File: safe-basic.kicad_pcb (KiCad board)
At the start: 10 x 10 mm, 1 part

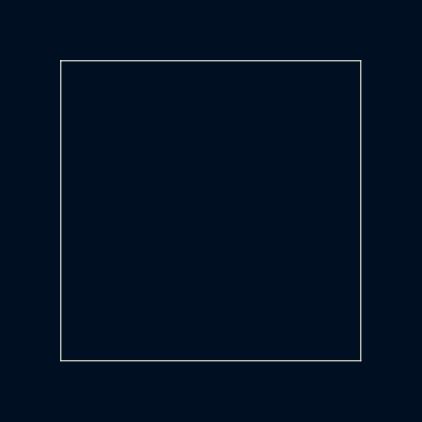
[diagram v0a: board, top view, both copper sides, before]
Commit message: test: source-authentic KiCad DRC track markers for #1161
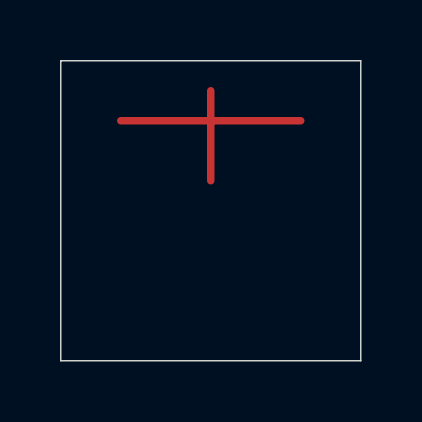
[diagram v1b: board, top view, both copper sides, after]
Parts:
- removed R1: , Resistor_SMD:R_0603
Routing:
- net NET_A: track 0.00 -> 6.00 mm
- net NET_B: track 0.00 -> 3.00 mm
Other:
- copper layers 0 -> 2
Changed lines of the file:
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@@
 (kicad_pcb
   (version 20250114)
-  (title_block (title "safe-basic") (rev "v1.0"))
-  (gr_rect (start 0 0) (end 10 10) (layer "Edge.Cuts"))
-  (footprint "Resistor_SMD:R_0603"
-    (property "Reference" "R1")
+  (generator "pcbnew")
+  (general (thickness 1.6))
+  (paper "A4")
+  (layers
+    (0 "F.Cu" signal)
+    (31 "B.Cu" signal)
+    (44 "Edge.Cuts" user)
   )
+  (setup (pad_to_mask_clearance 0))
+  (net 0 "")
+  (net 1 "NET_A")
+  (net 2 "NET_B")
+  (gr_rect (start 0 0) (end 10 10)
+    (stroke (width 0.05) (type default))
+    (fill none)
+    (layer "Edge.Cuts")
+  )
+  (segment (start 2 2) (end 8 2) (width 0.25) (layer "F.Cu") (net 1)
 )
+  (segment (start 5 1) (end 5 4) (width 0.25) (layer "F.Cu") (net 2)
+)
+)
